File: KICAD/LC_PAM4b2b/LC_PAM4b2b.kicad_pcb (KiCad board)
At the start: 4 copper layers, 120 x 26 mm, 18 parts, among them J1 Conn_01x02_Male, J10 Micro_SD_Board, J2 Conn_01x02_Male, J3 Conn_01x03_Pin, J4 Conn_01x02_Pin, J6 RTC, J7 Conn_01x03_Pin

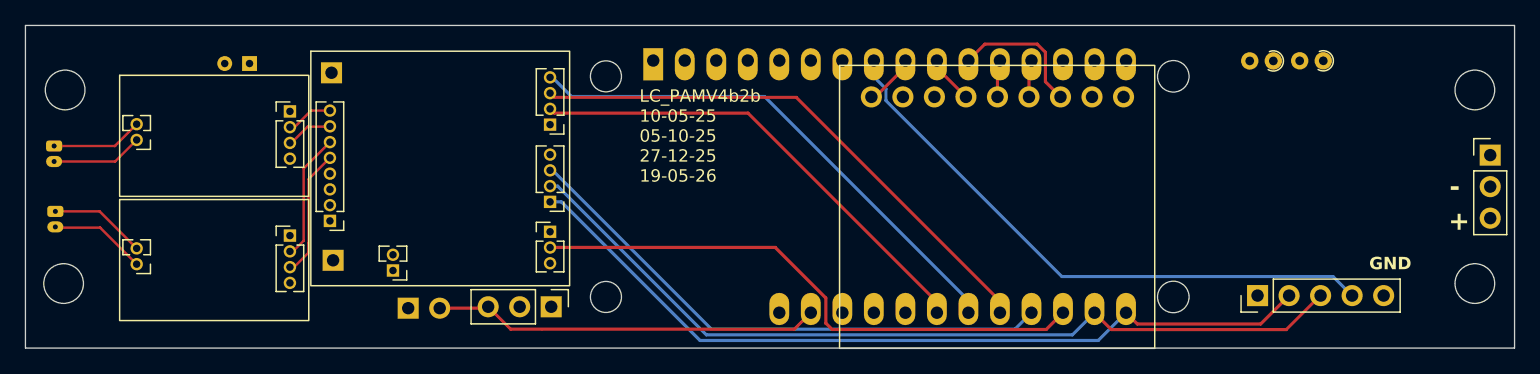
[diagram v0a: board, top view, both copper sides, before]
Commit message: corrected hibernate
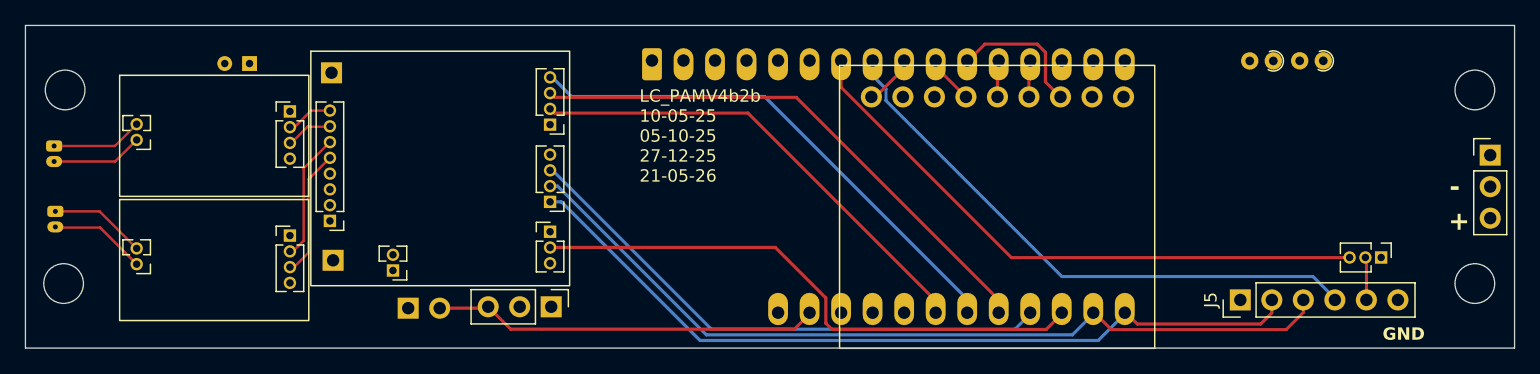
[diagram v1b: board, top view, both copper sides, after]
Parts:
- removed A1: Adafruit_Feather_RP2350, Module:Adafruit_Feather_WithMountingHoles
- added A2: Adafruit_Feather_RP2350, Module:Adafruit_Feather, B.Cu at (150.0, 84.7)
- added J5: Conn_01x06_Pin, Connector_PinHeader_2.54mm:PinHeader_1x06_P2.54mm_Vertical, F.Cu at (197.4, 104.0)
- J6: value RTC -> Conn_01x03_Pin; footprint Connector_PinHeader_2.54mm:PinHeader_1x05_P2.54mm_Vertical -> Connector_PinHeader_1.27mm:PinHeader_1x03_P1.27mm_Vertical
- moved J6 10.4 mm to (208.8, 100.6), turned to -90 degrees
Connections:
- J6 pad 1: /IOVD -> /GND
- J6 pad 2: /SDA0 -> /CLK
- J6 pad 3: /SCL0 -> Net-(A2-D27/A2)
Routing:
- net Net-(A2-D27/A2): track 0.00 -> 48.8 mm
- net /CLK: track 0.00 -> 3.69 mm
- net /nINT: track 47.7 -> 46.5 mm
- net /SDA0: track 66.4 -> 65.5 mm
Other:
- board text added: "LC_PAMV4b2b 10-05-25 05-10-25 27-12-25 21-05-26"
- board text removed: "LC_PAMV4b2b 10-05-25 05-10-25 27-12-25 19-05-26"
